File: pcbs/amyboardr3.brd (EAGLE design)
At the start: 100 x 80 mm, 109 parts, among them M13 M2.5, M14 M2.5, M15 M2.5, M16 M2.5, Q2 S8050, Q5 S8050, SW2 JS102011JAQN, U1 PCM9211PT, U13 HX3608, U14 CH340K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

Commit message: moving to 3.5mm jacks for everything
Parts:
- removed AUDIO_INPUT: 19269, microbuilder:4UCONN_19269
- removed SPDIFIN, SPDIFOUT: PJRAS1X1S01, PJRAS1X1S01:SWITCHCRAFT_PJRAS1X1S01
- added J11, J12, J13, J14, J15, J16, J17, J18, J19, J20: SJ1-3543, SJ1-3543:CUI_SJ1-3543
- moved MIDI_IN_CONN1 63.6 mm to (85.6, 16.3)
- moved SW2 61.9 mm to (49.7, 45.4)
- moved C90 57.5 mm to (106.2, 47.2)
- moved C86 53.2 mm to (101.3, 40.1)
- moved C87 53.2 mm to (107.7, 40.1)
- moved C88 53.2 mm to (79.8, 33.8)
- moved C91 53.2 mm to (98.8, 33.8)
- moved C96 53.2 mm to (105.2, 33.8)
- moved C97 53.2 mm to (79.8, 31.2)
- moved I2C1 53.2 mm to (48.0, 35.1)
- moved L4 53.2 mm to (103.9, 26.2)
- moved M16 53.2 mm to (44.2, 28.7)
- moved PCM5101 53.2 mm to (93.7, 24.9)
- moved R80 53.2 mm to (97.5, 40.1)
- moved U14 53.2 mm to (50.5, 21.1)
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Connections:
- net AGND: now also J11.1; no longer AUDIO_INPUT.1
- net BCLK: now also J20.2
- net GND: no longer SPDIFIN.G, SPDIFIN.S, SPDIFOUT.G, SPDIFOUT.S
- net LIN: now also J11.2; no longer AUDIO_INPUT.2, AUDIO_INPUT.4
- net LINX: now also J20.1
- net RIN: now also J11.3; no longer AUDIO_INPUT.3, AUDIO_INPUT.5
- net RINX: now also J20.3
- net SPDIFIN_SIGNAL: no longer SPDIFIN.T
- net SPDIFOUT_SIGNAL: no longer SPDIFOUT.T
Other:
- board size 100 x 80 mm -> 129 x 50.5 mm

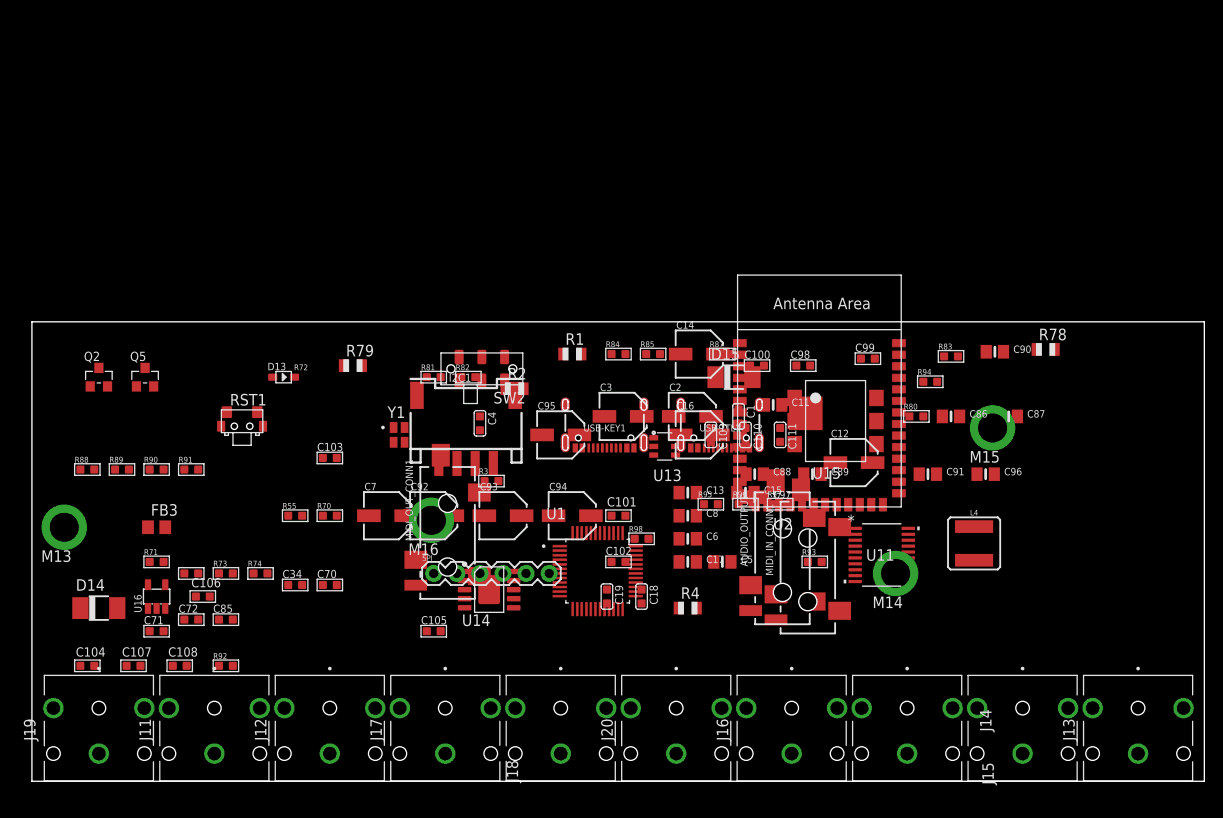
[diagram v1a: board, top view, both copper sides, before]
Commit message: stacked audio jacks
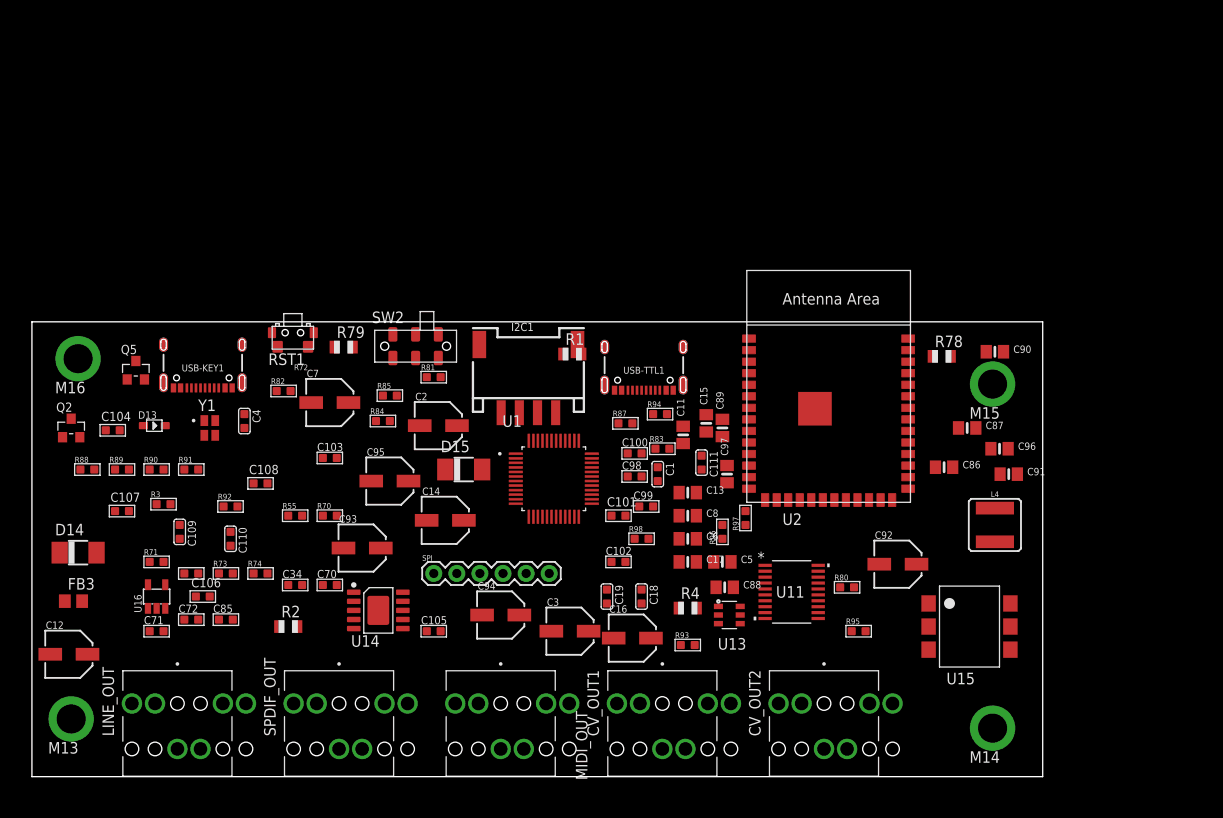
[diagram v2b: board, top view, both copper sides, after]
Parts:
- removed AUDIO_OUTPUT, MIDI_IN_CONN1, MIDI_OUT_CONN1: 19269, microbuilder:4UCONN_19269
- removed J11, J12, J13, J14, J15, J16, J17, J18, J19, J20: SJ1-3543, SJ1-3543:CUI_SJ1-3543
- added CV_IN1, CV_IN2, CV_OUT1, CV_OUT2, LINE_IN, LINE_OUT, MIDI_IN, MIDI_OUT, SPDIF_IN, SPDIF_OUT: SJ1-3543, SJ1-3543:CUI_SJ1-3543
- moved C12 88.9 mm to (4.32, 14.0)
- moved C109 59.4 mm to (16.5, 27.4)
- moved C110 57.8 mm to (22.1, 26.7)
- moved C92 51.3 mm to (95.5, 23.9)
- moved USB-KEY1 44.7 mm to (19.1, 42.9)
- moved M16 42.7 mm to (5.33, 46.5)
- moved R3 36.2 mm to (14.7, 30.5)
- moved R2 36.1 mm to (28.4, 17.0)
- moved C14 33.4 mm to (45.7, 28.7)
- moved R83 33.3 mm to (69.6, 36.6)
- moved D15 31.4 mm to (47.8, 34.3)
- moved R94 29.9 mm to (69.3, 40.4)
- moved R85 29.3 mm to (39.6, 42.4)
- moved C99 29.3 mm to (67.8, 30.2)
- moved C2 28.0 mm to (45.0, 39.1)
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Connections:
- removed net IO15: U2.8
- removed net IO16: U2.9
- removed net IO38: U2.31
- removed net IO39: U2.32
- new net ADC0: CV_IN2.2, U2.8
- new net ADC1: CV_IN1.2, U2.9
- new net N$10: SPDIF_IN.3
- new net N$11: CV_OUT1.3
- new net N$12: CV_OUT2.3
- new net N$13: CV_IN1.3
- new net N$14: CV_IN2.3
- new net N$9: SPDIF_OUT.3
- new net PWM0: CV_OUT1.2, U2.31
- new net PWM1: CV_OUT2.2, U2.32
- net AGND: now also LINE_IN.1, LINE_OUT.1; no longer AUDIO_OUTPUT.1, J11.1
- net BCLK: no longer J20.2
- net GND: now also CV_IN1.1, CV_IN2.1, CV_OUT1.1, CV_OUT2.1, MIDI_IN.1, MIDI_OUT.1, SPDIF_IN.1, SPDIF_OUT.1; no longer MIDI_IN_CONN1.1, MIDI_OUT_CONN1.1
- net LIN: now also LINE_IN.2; no longer J11.2
- net LINX: no longer J20.1
- net LOUT: now also LINE_OUT.2; no longer AUDIO_OUTPUT.2, AUDIO_OUTPUT.4
- net N$55: now also MIDI_IN.2; no longer MIDI_IN_CONN1.2, MIDI_IN_CONN1.4
- net N$56: now also MIDI_IN.3; no longer MIDI_IN_CONN1.3, MIDI_IN_CONN1.5
- net N$58: now also MIDI_OUT.2; no longer MIDI_OUT_CONN1.2, MIDI_OUT_CONN1.4
- net N$59: now also MIDI_OUT.3; no longer MIDI_OUT_CONN1.3, MIDI_OUT_CONN1.5
- net RIN: now also LINE_IN.3; no longer J11.3
- net RINX: no longer J20.3
- net ROUT: now also LINE_OUT.3; no longer AUDIO_OUTPUT.3, AUDIO_OUTPUT.5
- net SPDIFIN_SIGNAL: now also SPDIF_IN.2
- net SPDIFOUT_SIGNAL: now also SPDIF_OUT.2
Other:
- board size 129 x 50.5 mm -> 111.2 x 50 mm

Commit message: dac/adcs
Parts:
- added C10, C9: 10nF, Discrete-new:C0603
- added MABEEDAC: (no value), SparkFun-Connectors:1X04
- added R5, R7: 68K, adafruit:R0805
- added R6, R8: 33K, adafruit:R0805
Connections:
- new net MABEEDAC_VOUT0: CV_OUT1.2, MABEEDAC.3
- new net MABEEDAC_VOUT1: CV_OUT2.2, MABEEDAC.4
- new net N$15: CV_OUT2.1
- new net N$16: C9.1, CV_IN2.2, R7.2, R8.1
- new net N$18: C10.1, CV_IN1.2, R5.2, R6.1
- net +3V3: now also MABEEDAC.2
- net ADC0: now also R5.1; no longer CV_IN2.2
- net ADC1: now also R7.1; no longer CV_IN1.2
- net GND: now also C10.2, C9.2, MABEEDAC.1, R6.2, R8.2; no longer CV_OUT2.1
- net PWM0: no longer CV_OUT1.2
- net PWM1: no longer CV_OUT2.2

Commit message: header, fixed adcs
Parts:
- added J1: 52601-G10-8LF, 52601-G10-8LF:AMPHENOL_52601-G10-8LF
- C10, C9: value 10nF -> 1nF
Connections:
- removed net N$16: C9.1, CV_IN2.2, R7.2, R8.1
- removed net N$18: C10.1, CV_IN1.2, R5.2, R6.1
- new net +12V: J1.09, J1.10
- new net -12V: J1.01, J1.02
- new net N$17: CV_IN1.2, R5.1
- new net N$19: CV_IN2.2, R7.1
- net ADC0: now also C10.1, R5.2, R6.1; no longer R5.1
- net ADC1: now also C9.1, R7.2, R8.1; no longer R7.1
- net GND: now also J1.03, J1.04, J1.05, J1.06, J1.07, J1.08
